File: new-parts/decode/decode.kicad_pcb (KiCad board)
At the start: 2 copper layers, 132.1 x 63.5 mm, 37 parts, among them J1 BHR-10-VUA, J10 Conn_02x01, J11 Conn_02x01, J12 Conn_02x01, J13 Conn_02x01, J14 Conn_02x01, J2 Conn_02x01, J3 Conn_02x01, J4 Conn_02x01, J5 Conn_02x01, J6 Conn_02x03_Odd_Even, J7 Conn_02x01, J8 Conn_02x01, J9 Conn_02x01, K1 J104D2C12VDC.15S, K2 J104D2C12VDC.15S, K3 J104D2C12VDC.15S, K4 J104D2C12VDC.15S, K5 J104D2C12VDC.15S, K6 J104D2C12VDC.15S, K7 J104D2C12VDC.15S, K8 J104D2C12VDC.15S, K9 J104D2C12VDC.15S

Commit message: Layout decoder.
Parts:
- added TP2: TestPoint, TestPoint:TestPoint_Pad_D1.5mm, F.Cu at (139.7, 31.8)
- added TP3: TestPoint, TestPoint:TestPoint_Pad_D1.5mm, F.Cu at (143.5, 31.8)
- added TP4: TestPoint, TestPoint:TestPoint_Pad_D1.5mm, F.Cu at (147.3, 31.8)
- added TP5: TestPoint, TestPoint:TestPoint_Pad_D1.5mm, F.Cu at (151.1, 31.8)
- added TP6: TestPoint, TestPoint:TestPoint_Pad_D1.5mm, F.Cu at (154.9, 31.8)
- added TP7: TestPoint, TestPoint:TestPoint_Pad_D1.5mm, F.Cu at (158.8, 31.8)
- added TP8: TestPoint, TestPoint:TestPoint_Pad_D1.5mm, F.Cu at (162.6, 31.8)
- D1, D11, D12, D2, D3, D4, D5, D6, D7, D8, D9: moved to B.Cu
- moved J2 96.5 mm to (188.0, 44.5), turned to 180 degrees
- moved J6 90.3 mm to (193.0, 100.3), turned to -90 degrees
- moved J7 83.9 mm to (199.4, 100.3), turned to 0 degrees
- moved J14 82.4 mm to (142.2, 38.1)
- moved K1 73.7 mm to (179.1, 41.9), turned to 180 degrees
- moved J3 69.4 mm to (142.2, 43.2)
- moved J4 69.4 mm to (142.2, 48.3)
- moved K7 65.1 mm to (208.3, 77.5), turned to 0 degrees
- moved D9 62.1 mm to (218.4, 48.3), turned to 90 degrees
- moved D8 61.5 mm to (222.2, 48.3), turned to 90 degrees
- moved D7 61.0 mm to (226.1, 48.3), turned to 90 degrees
- moved J13 57.5 mm to (142.2, 53.3)
- moved D1 55.7 mm to (175.3, 45.7), turned to 90 degrees
- moved D11 48.3 mm to (212.1, 86.4), turned to -90 degrees
- moved K8 48.3 mm to (208.3, 90.2), turned to 0 degrees
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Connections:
- J3 pad 1: /a en out -> /p en out
- J4 pad 1: /p en out -> /a en out
- K1 pad 11: /a en out -> /p en out
- K1 pad 14: a en -> p en
- K1 pad 21: /p en out -> /a en out
- K1 pad 24: p en -> a en
- K3 pad 11: Net-(K3-Pad11) -> Net-(D4-A2)
- K3 pad 12: GND -> Net-(K2-Pad11)
- K3 pad 14: VCC -> Net-(K2-Pad21)
- K3 pad A1: Net-(D4-A2) -> c2
- K3 pad A2: cinv -> GND
- K4 pad 11: Net-(D4-A2) -> Net-(K4-Pad11)
- K4 pad 12: Net-(K2-Pad11) -> GND
- K4 pad 14: Net-(K2-Pad21) -> VCC
- K4 pad A1: c2 -> Net-(D4-A2)
- K4 pad A2: GND -> cinv
- K5 pad 14: Net-(K3-Pad11) -> Net-(K4-Pad11)
- K9 pad 11: cf -> unconnected-(K9-Pad11)
- K9 pad 12: GND -> unconnected-(K9-Pad12)
- K9 pad 14: VCC -> unconnected-(K9-Pad14)
- K9 pad 21: unconnected-(K9-Pad21) -> cf
- K9 pad 22: unconnected-(K9-Pad22) -> GND
- K9 pad 24: unconnected-(K9-Pad24) -> VCC
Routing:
- net m en: track 31.0 -> 163.5 mm, vias 1 -> 2
- net a en: track 31.0 -> 161.5 mm, vias 1 -> 3
- net add: track 46.2 -> 167.5 mm, vias 1 -> 4
- net p en: track 41.5 -> 162.0 mm, vias 1 -> 3
- net clk: track 23.5 -> 71.1 mm
- net cf: track 0.00 -> 45.6 mm
- net Net-(D12-A2): track 56.2 -> 22.2 mm, vias 1 -> 0
- net c2: track 66.9 -> 100.6 mm, vias 1 -> 4
- net Net-(K5-Pad11): track 17.3 -> 47.6 mm
- net Net-(K4-Pad11): track 0.00 -> 24.2 mm
- net Net-(D11-A2): track 4.40 -> 25.0 mm
- net Net-(K8-Pad12): track 2.77 -> 23.3 mm
- net zf: track 30.1 -> 10.0 mm
- net Net-(K3-Pad11): track 19.4 -> 0.00 mm
- net Net-(C1-Pad1): track 0.00 -> 19.4 mm
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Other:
- board size 132.1 x 63.5 mm -> 96.5 x 82.5 mm
- board text added: "a enable"
- board text added: "adder"
- board text added: "addr src"
- board text added: "carry in"
- board text added: "clk in"
- board text added: "control out"
- board text added: "flags in"
- board text added: "insn in"
- board text added: "invert"
- board text added: "mem write"
- board text added: "od"
- board text added: "operand src"
- board text added: "p enable"
- board text added: "pc source (jump)"
- board text added: "res src 1"
- board text added: "res src 2"
- board text added: "s"
- board text added: "z"
- board text removed: "Flags"
- board text removed: "Insn"

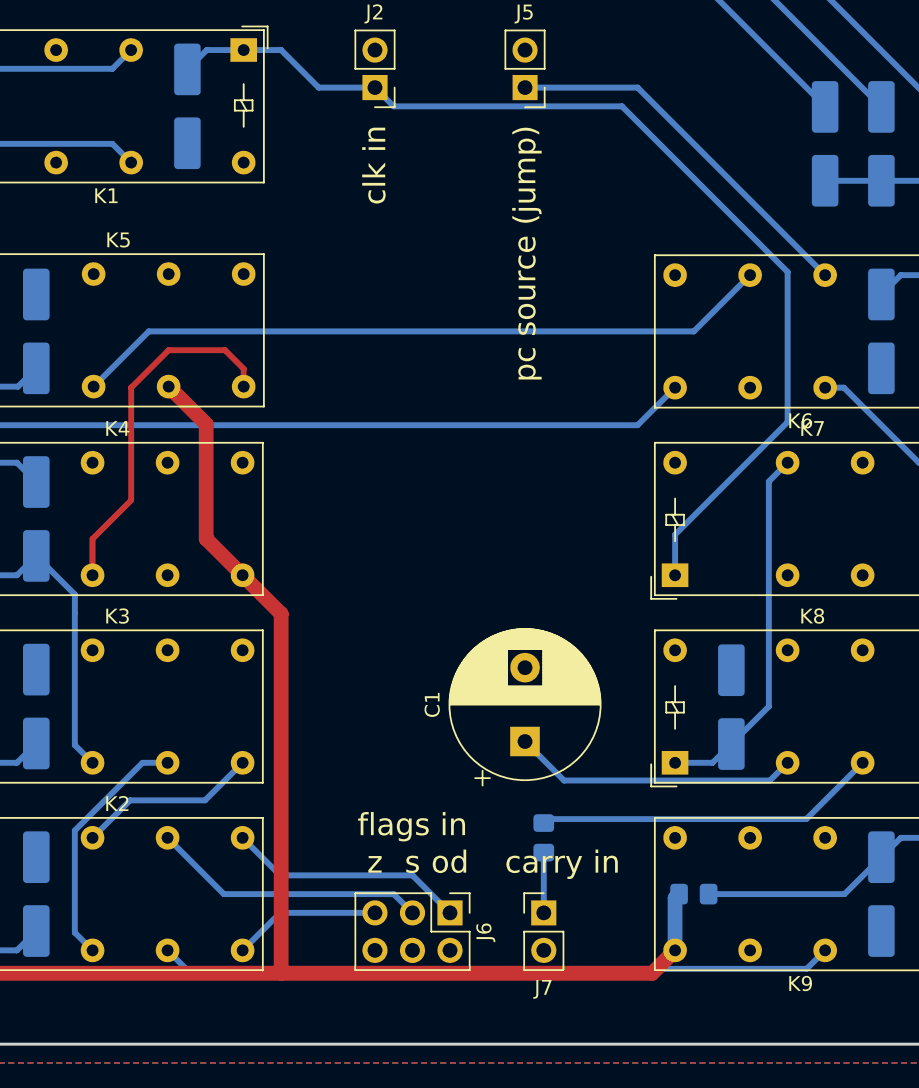
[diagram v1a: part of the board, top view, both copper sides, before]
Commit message: decode: Position silkscreen labels, strengthen flags's ground connection.
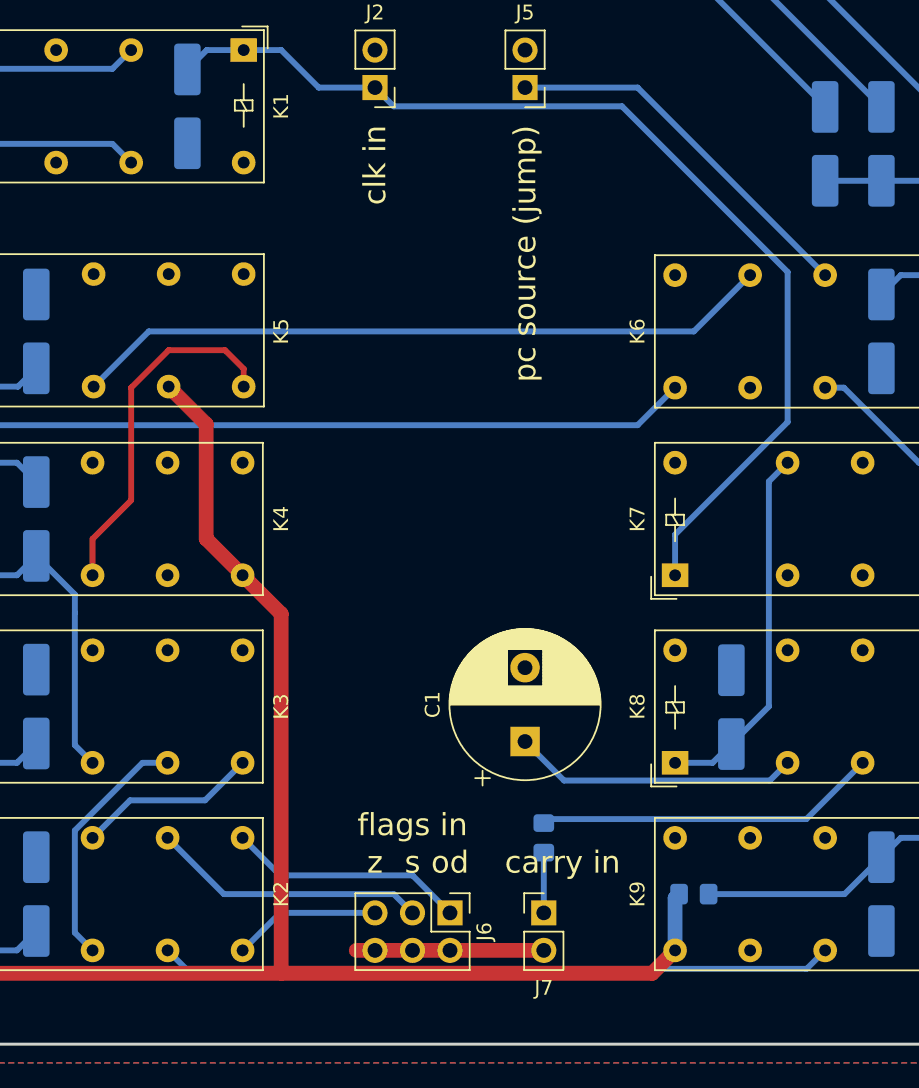
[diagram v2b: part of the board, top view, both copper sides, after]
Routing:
- net GND: track 0.00 -> 12.7 mm
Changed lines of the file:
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@@
     (property "ki_keywords" "Relay DPDT")
     (attr through_hole)
-    (fp_text reference "K4" (at 9.3 -9.9) (layer "F.SilkS")
+    (fp_text reference "K4" (at 20.3925 -3.81 90) (layer "F.SilkS")
         (effects (font (size 1 1) (thickness 0.15)))
     )
@@
     (property "ki_keywords" "Relay DPDT")
     (attr through_hole)
-    (fp_text reference "K9" (at 9.3 -9.9) (layer "F.SilkS")
+    (fp_text reference "K9" (at 20.32 -3.81 90) (layer "F.SilkS")
         (effects (font (size 1 1) (thickness 0.15)))
     )
@@
     (property "ki_keywords" "Relay DPDT")
     (attr through_hole)
-    (fp_text reference "K8" (at 9.3 -9.9) (layer "F.SilkS")
+    (fp_text reference "K8" (at -2.54 -3.81 90) (layer "F.SilkS")
         (effects (font (size 1 1) (thickness 0.15)))
     )
@@
     (property "ki_keywords" "Relay DPDT")
     (attr through_hole)
-    (fp_text reference "K2" (at 9.3 -9.9) (layer "F.SilkS")
+    (fp_text reference "K2" (at 20.3925 -3.81 90) (layer "F.SilkS")
         (effects (font (size 1 1) (thickness 0.15)))
     )
@@
     (property "ki_keywords" "Relay DPDT")
     (attr through_hole)
-    (fp_text reference "K3" (at 9.3 -9.9) (layer "F.SilkS")
+    (fp_text reference "K3" (at 20.3925 -3.81 90) (layer "F.SilkS")
         (effects (font (size 1 1) (thickness 0.15)))
     )
@@
     (property "ki_keywords" "Relay DPDT")
     (attr through_hole)
-    (fp_text reference "K1" (at 9.3 -9.9) (layer "F.SilkS")
+    (fp_text reference "K1" (at -2.54 -3.81 90) (layer "F.SilkS")
         (effects (font (size 1 1) (thickness 0.15)))
     )
@@
     (property "ki_keywords" "Relay DPDT")
     (attr through_hole)
-    (fp_text reference "K7" (at 9.3 -9.9) (layer "F.SilkS")
+    (fp_text reference "K7" (at -2.54 -3.81 90) (layer "F.SilkS")
         (effects (font (size 1 1) (thickness 0.15)))
     )
@@
     (property "ki_keywords" "Relay DPDT")
     (attr through_hole)
-    (fp_text reference "K5" (at 9.3 -9.9) (layer "F.SilkS")
+    (fp_text reference "K5" (at 20.32 -3.7375 90) (layer "F.SilkS")
         (effects (font (size 1 1) (thickness 0.15)))
     )
@@
     (property "ki_keywords" "Relay DPDT")
     (attr through_hole)
-    (fp_text reference "K6" (at 9.3 -9.9) (layer "F.SilkS")
+    (fp_text reference "K6" (at 20.32 -3.81 90) (layer "F.SilkS")
         (effects (font (size 1 1) (thickness 0.15)))
     )
@@
     (property "ki_keywords" "diode")
     (attr smd)
-    (fp_text reference "D8" (at 0 2.5 90) (layer "B.SilkS")
+    (fp_text reference "D8" (at 5.715 0 180) (layer "B.SilkS")
         (effects (font (size 1 1) (thickness 0.15)) (justify mirror))
     )
@@
     (property "ki_keywords" "diode")
     (attr smd)
-    (fp_text reference "D9" (at 0 2.5 90) (layer "B.SilkS")
+    (fp_text reference "D9" (at 5.715 0 180) (layer "B.SilkS")
         (effects (font (size 1 1) (thickness 0.15)) (justify mirror))
     )
@@
     (property "ki_keywords" "diode")
     (attr smd)
-    (fp_text reference "D7" (at 0 2.5 90) (layer "B.SilkS")
+    (fp_text reference "D7" (at 5.715 0 180) (layer "B.SilkS")
         (effects (font (size 1 1) (thickness 0.15)) (justify mirror))
     )
@@
   (segment (start 208.28 102.87) (end 208.28 99.33) (width 1) (layer "B.Cu") (net 15))
   (segment (start 208.28 99.33) (end 208.55 99.06) (width 1) (layer "B.Cu") (net 15))
+  (segment (start 187.96 102.87) (end 186.69 102.87) (width 1) (layer "F.Cu") (net 16))
+  (segment (start 190.5 102.87) (end 193.04 102.87) (width 1) (layer "F.Cu") (net 16))
+  (segment (start 193.04 102.87) (end 199.39 102.87) (width 1) (layer "F.Cu") (net 16))
+  (segment (start 187.96 102.87) (end 190.5 102.87) (width 1) (layer "F.Cu") (net 16))
   (segment (start 215.9 69.85) (end 214.63 71.12) (width 0.4) (layer "B.Cu") (net 17))
   (segment (start 212.09 88.9) (end 210.82 90.17) (width 0.4) (layer "B.Cu") (net 17))

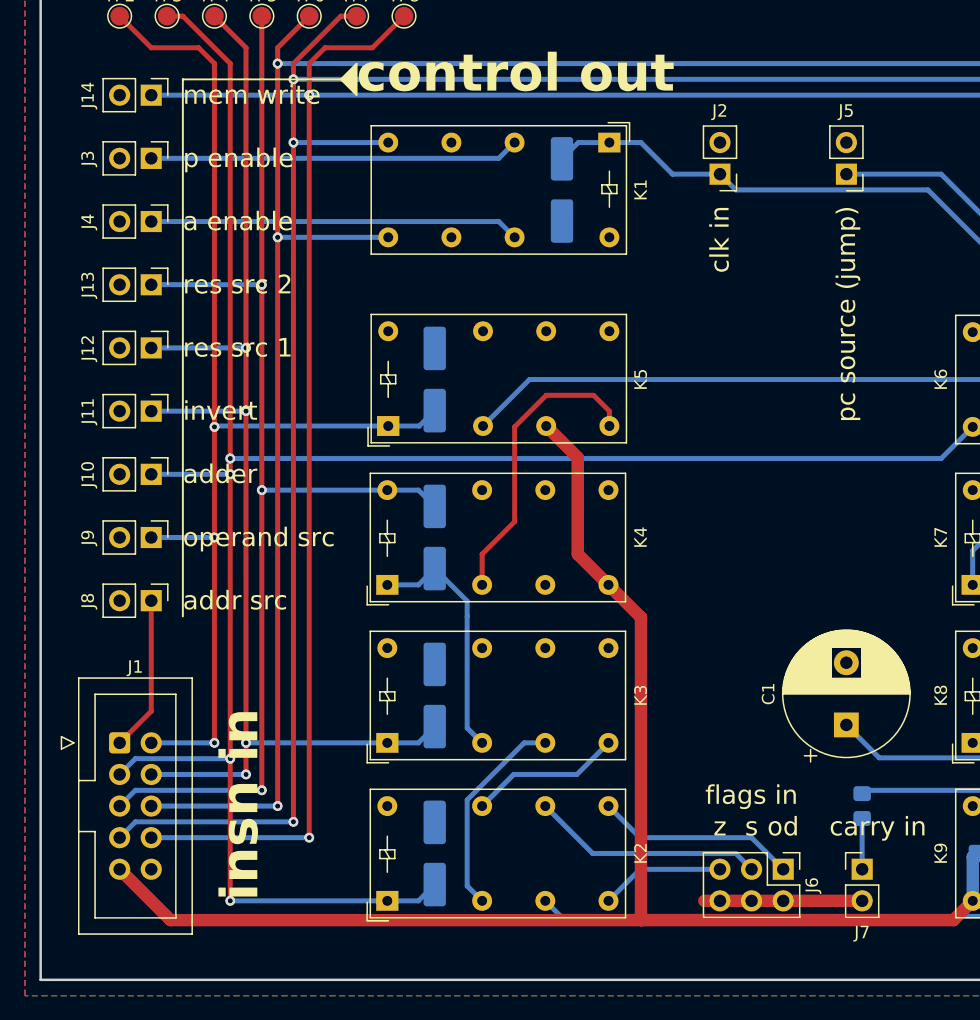
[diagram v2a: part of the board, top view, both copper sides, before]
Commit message: Change all two-pin headers for control + ground to control only.
This is to prevent accidental short circuits when they are plugged in the
wrong way.
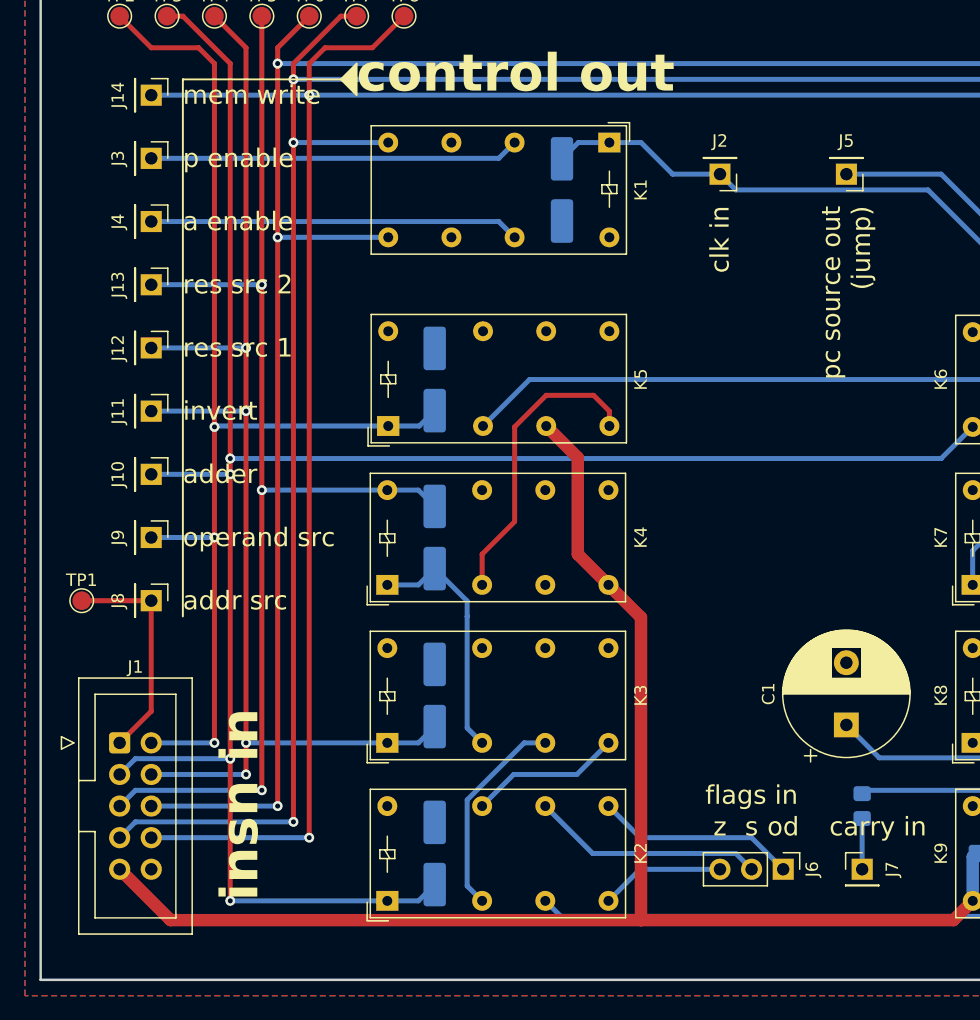
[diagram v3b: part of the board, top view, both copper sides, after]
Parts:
- added TP1: TestPoint, TestPoint:TestPoint_Pad_D1.5mm, F.Cu at (136.7, 78.7)
- J10, J11, J12, J13, J14, J2, J3, J4, J5, J7, J8, J9: footprint Connector_PinHeader_2.54mm:PinHeader_1x02_P2.54mm_Vertical -> Connector_PinHeader_2.54mm:PinHeader_1x01_P2.54mm_Vertical
- J6: footprint Connector_PinHeader_2.54mm:PinHeader_2x03_P2.54mm_Vertical -> Connector_PinHeader_2.54mm:PinHeader_1x03_P2.54mm_Vertical
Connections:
- J6 pad 2: GND -> sf
- J6 pad 3: sf -> zf
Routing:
- net GND: track 12.7 -> 0.00 mm
- net as: track 12.5 -> 18.1 mm
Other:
- board text added: "pc source out (jump)"
- board text removed: "pc source (jump)"

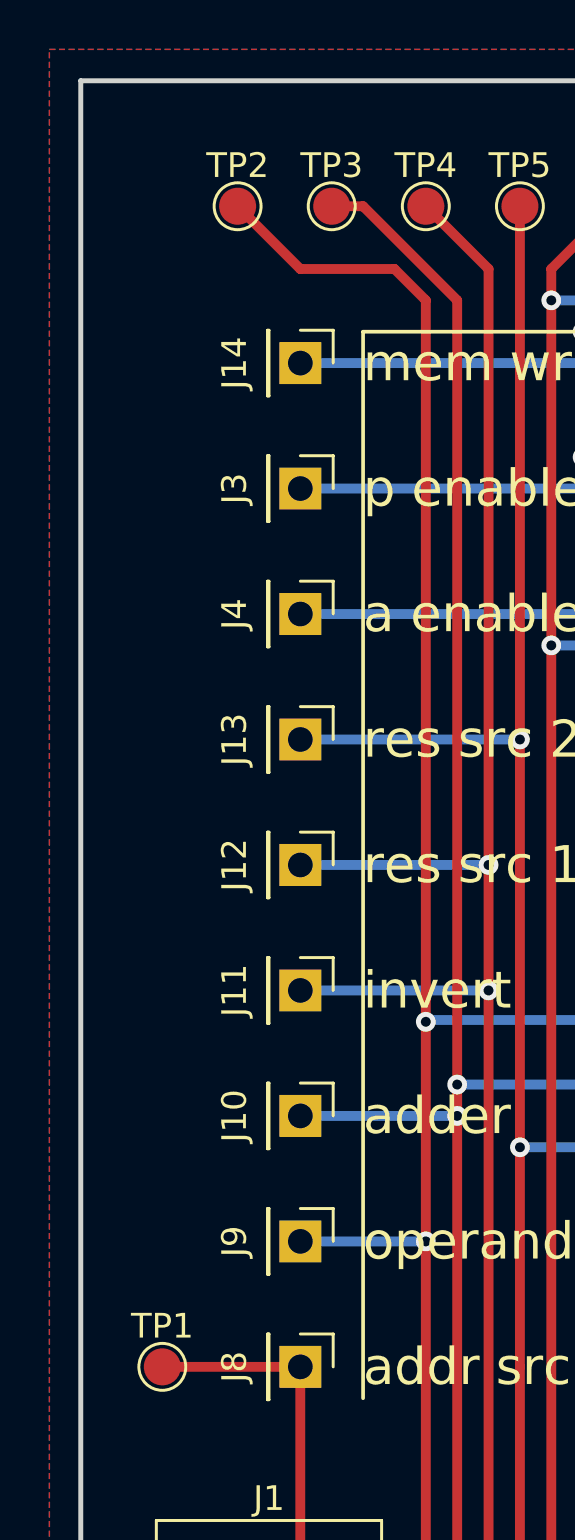
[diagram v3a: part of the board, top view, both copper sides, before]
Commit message: decode: Move TP1 to join the others.
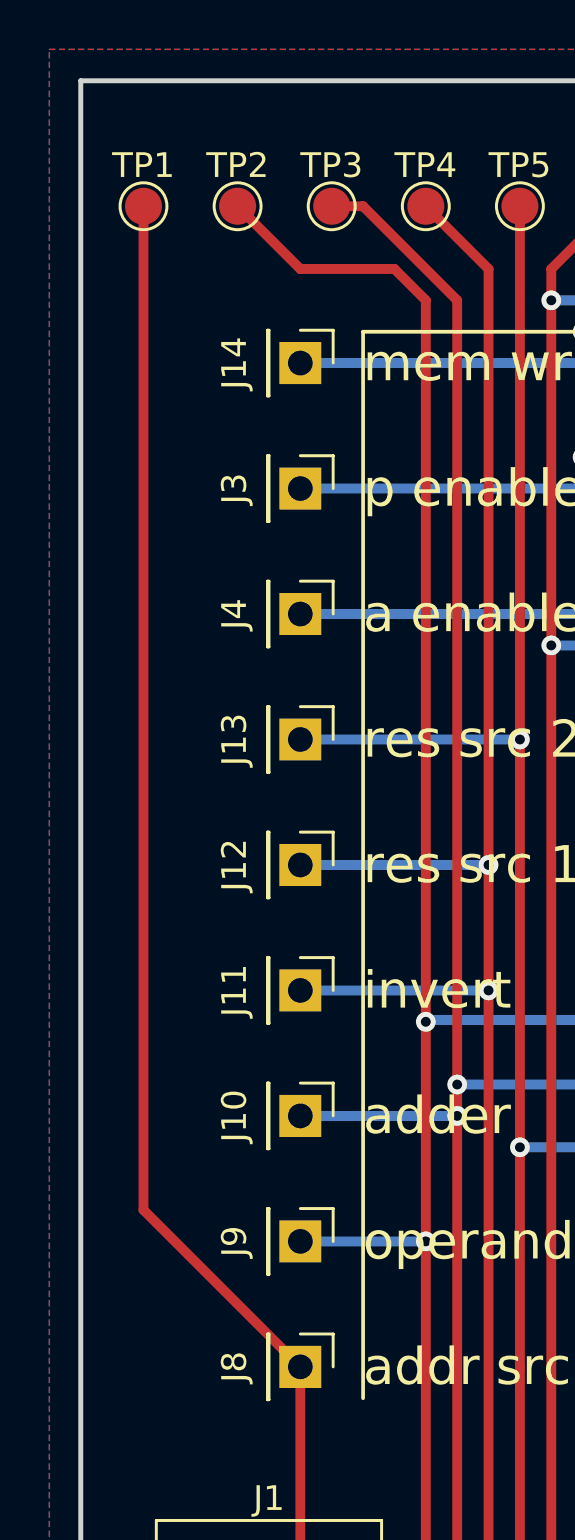
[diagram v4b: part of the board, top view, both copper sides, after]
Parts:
- moved TP1 47.0 mm to (135.9, 31.8)
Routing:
- net as: track 18.1 -> 62.1 mm
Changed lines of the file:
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@@
   )
   (footprint "TestPoint:TestPoint_Pad_D1.5mm" (layer "F.Cu")
-    (at 136.652 78.74)
+    (at 135.89 31.75)
     (descr "SMD pad as test Point, diameter 1.5mm")
     (tags "test point SMD pad")
@@
     (style (thickness 0.15) (arrow_length 1.27) (text_position_mode 0) (extension_height 0.58642) (extension_offset 0.5) keep_text_aligned)
   )
-  (segment (start 136.652 78.74) (end 142.24 78.74) (width 0.4) (layer "F.Cu") (net 1))
+  (segment (start 135.89 31.75) (end 135.89 72.39) (width 0.4) (layer "F.Cu") (net 1))
+  (segment (start 135.89 72.39) (end 142.24 78.74) (width 0.4) (layer "F.Cu") (net 1))
   (segment (start 142.24 78.74) (end 142.24 87.63) (width 0.4) (layer "F.Cu") (net 1))
   (segment (start 142.24 87.63) (end 139.7 90.17) (width 0.4) (layer "F.Cu") (net 1))

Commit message: Add placeholders for JLC order number.
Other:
- board text added: "JLCJLCJLCJLC"
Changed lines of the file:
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@@
   (gr_line (start 229.87 26.67) (end 229.87 109.22)
     (stroke (width 0.2) (type default)) (layer "Edge.Cuts"))
+  (gr_text "JLCJLCJLCJLC" (at 228.346 107.696) (layer "B.SilkS")
+    (effects (font (size 1 1) (thickness 0.15)) (justify left bottom mirror))
+  )
   (gr_text "res src 2" (at 144.78 53.34) (layer "F.SilkS")
     (effects (font (size 1.5 1.5) (thickness 0.1875)) (justify left))

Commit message: Add a "title" label to all parts.
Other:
- board text added: "vis vitalis instruction decoder"
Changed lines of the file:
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@@
   (gr_line (start 229.87 26.67) (end 229.87 109.22)
     (stroke (width 0.2) (type default)) (layer "Edge.Cuts"))
+  (gr_text "vis vitalis\ninstruction decoder" (at 228.346 36.83) (layer "B.SilkS")
+    (effects (font (size 3 3) (thickness 0.6) bold) (justify left bottom mirror))
+  )
   (gr_text "JLCJLCJLCJLC" (at 228.346 107.696) (layer "B.SilkS")
     (effects (font (size 1 1) (thickness 0.15)) (justify left bottom mirror))
